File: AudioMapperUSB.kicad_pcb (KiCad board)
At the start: 2 copper layers, 100 x 100 mm, 155 parts, among them J1 USB_B, J10 Conn_01x01, J11 Conn_01x01, J12 Jack-DC, J16 Audio-Jack-2, J17 Audio-Jack-2, J18 Audio-Jack-2, J19 Audio-Jack-2, J2 Audio-Jack-2, J20 Audio-Jack-2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

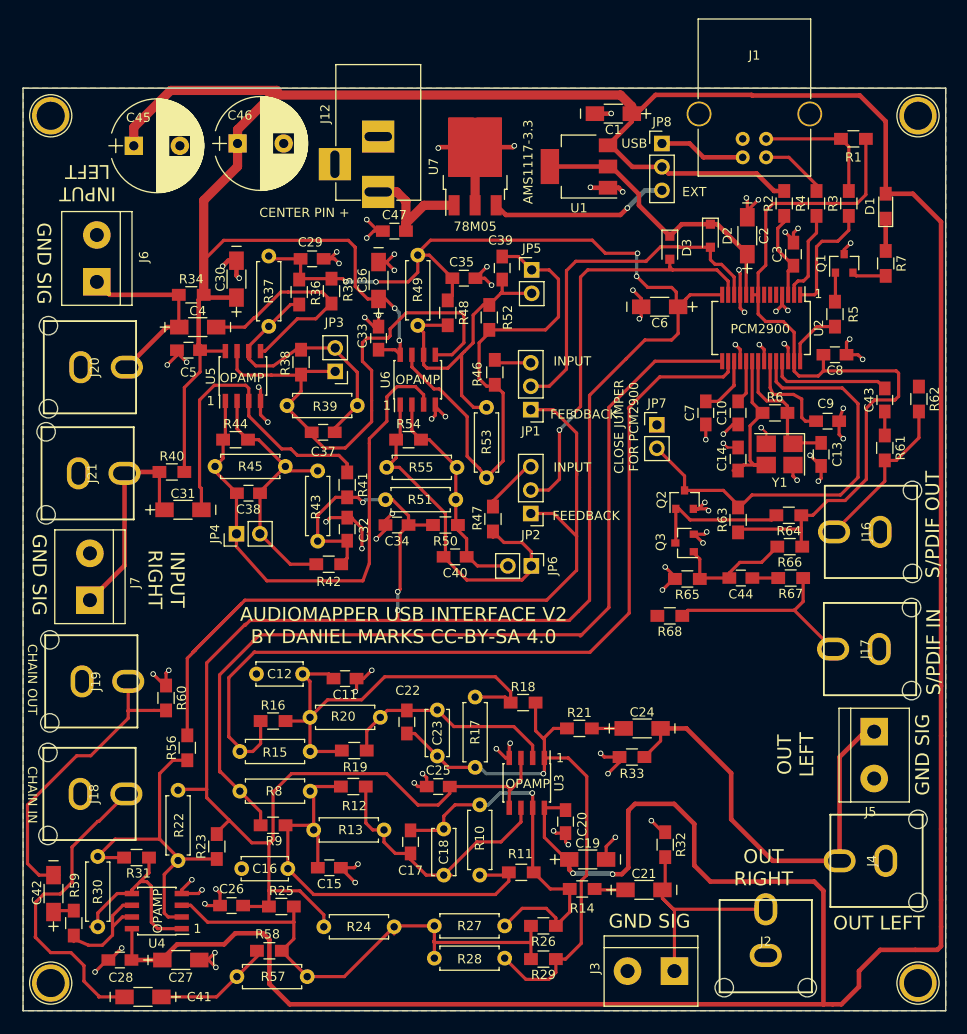
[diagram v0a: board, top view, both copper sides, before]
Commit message: Use inverter for SPDIF
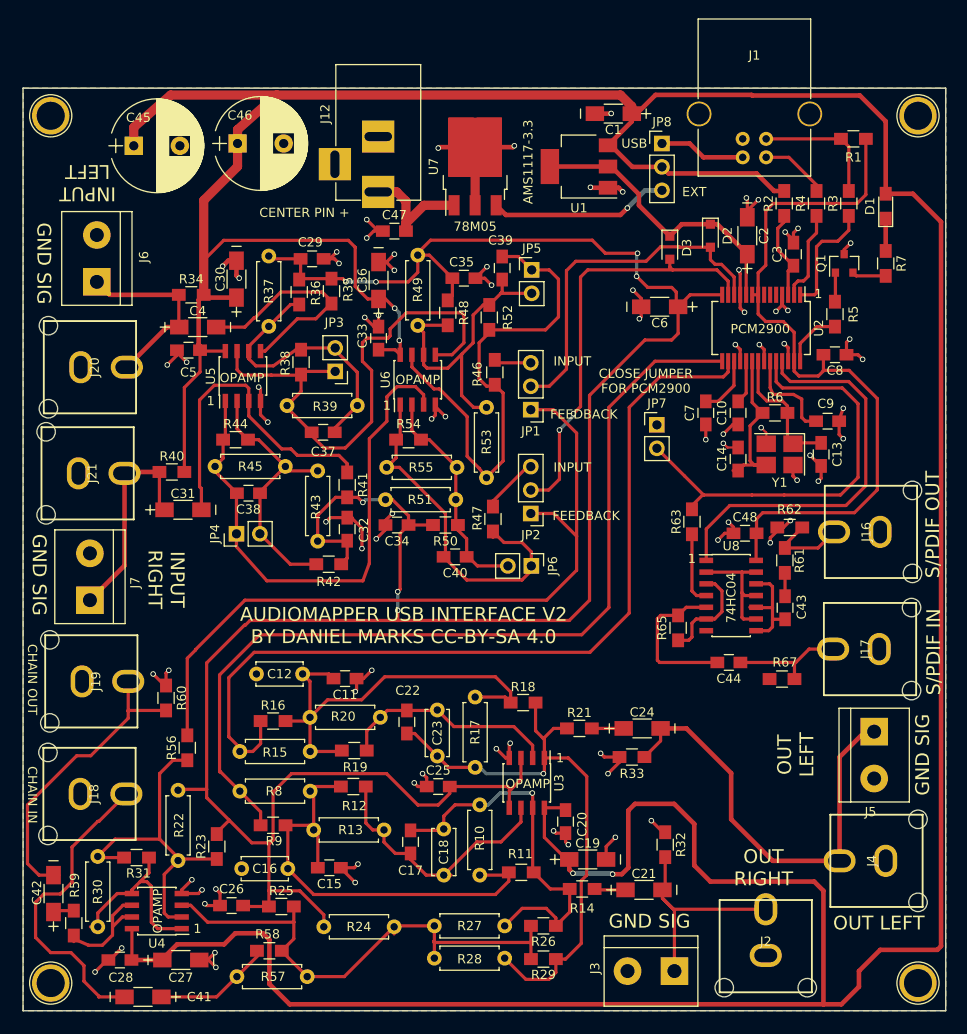
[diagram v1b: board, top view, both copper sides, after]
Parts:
- removed Q2, Q3: MMBT3904, TO_SOT_Packages_SMD:SOT-23
- removed R64: 1k, Resistors_SMD:R_0805_HandSoldering
- removed R66: 100k, Resistors_SMD:R_0805_HandSoldering
- removed R68: NC, Resistors_SMD:R_0805_HandSoldering
- added C48: 1 uF, Capacitors_SMD:C_0805_HandSoldering, F.Cu at (108.2, 78.2)
- added U8: 74HC04, Housings_SOIC:SOIC-14_3.9x8.7mm_Pitch1.27mm, F.Cu at (106.8, 85.0)
- R52, R54: value 100k -> 22k
- R65: value 10k -> 100k
- moved C43 25.0 mm to (112.6, 86.3), turned to 270 degrees
- moved R62 19.7 mm to (113.1, 77.6), turned to 0 degrees
- moved R61 16.3 mm to (112.6, 81.2), turned to 90 degrees
- moved R67 11.0 mm to (112.3, 94.0)
- moved C44 9.24 mm to (106.5, 92.2)
- moved R65 5.39 mm to (101.0, 88.5), turned to 270 degrees
- moved R63 5.00 mm to (102.5, 77.0)
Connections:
- C8 pad 1: Net-(C8-Pad1) -> VDDI
- J17 pad 1: Net-(J17-Pad1) -> Net-(C44-Pad1)
- R1 pad 2: Net-(C8-Pad1) -> VDDI
- R63 pad 1: Net-(C8-Pad1) -> Net-(R63-Pad1)
- R65 pad 2: GND -> Net-(R65-Pad2)
- R67 pad 1: Net-(J17-Pad1) -> Net-(C44-Pad1)
- R67 pad 2: Net-(C44-Pad1) -> GND
- U2 pad 25: Net-(C43-Pad2) -> Net-(U2-Pad25)
- U2 pad 27: Net-(C8-Pad1) -> VDDI
- U2 pad 8: Net-(C8-Pad1) -> VDDI
- U2 pad 9: Net-(C8-Pad1) -> VDDI
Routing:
- net Net-(C8-Pad1): track 86.2 -> 0.00 mm
- net VDDI: track 0.00 -> 80.8 mm
- net Net-(U2-Pad25): track 0.00 -> 43.6 mm
- net Net-(J17-Pad1): track 22.2 -> 0.00 mm
- net Net-(Q2-Pad1): track 15.3 -> 0.00 mm
- net Net-(U8-Pad11): track 0.00 -> 13.7 mm
- net Net-(R65-Pad2): track 0.00 -> 11.2 mm
- net Net-(C44-Pad1): track 2.80 -> 12.5 mm
- net Net-(J16-Pad1): track 17.6 -> 9.30 mm
- net Net-(JP1-Pad1): track 89.5 -> 81.4 mm
- net Net-(R63-Pad1): track 0.00 -> 7.91 mm
- net GND: track 174.8 -> 171.2 mm, vias 82 -> 80
- net Net-(C44-Pad2): track 13.4 -> 16.9 mm
- net Net-(C1-Pad1): track 466.7 -> 464.8 mm
- net Net-(C43-Pad2): track 13.3 -> 12.1 mm
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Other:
- board text added: "74HC04"

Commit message: Fixed problem with VCOM leaking into input audio
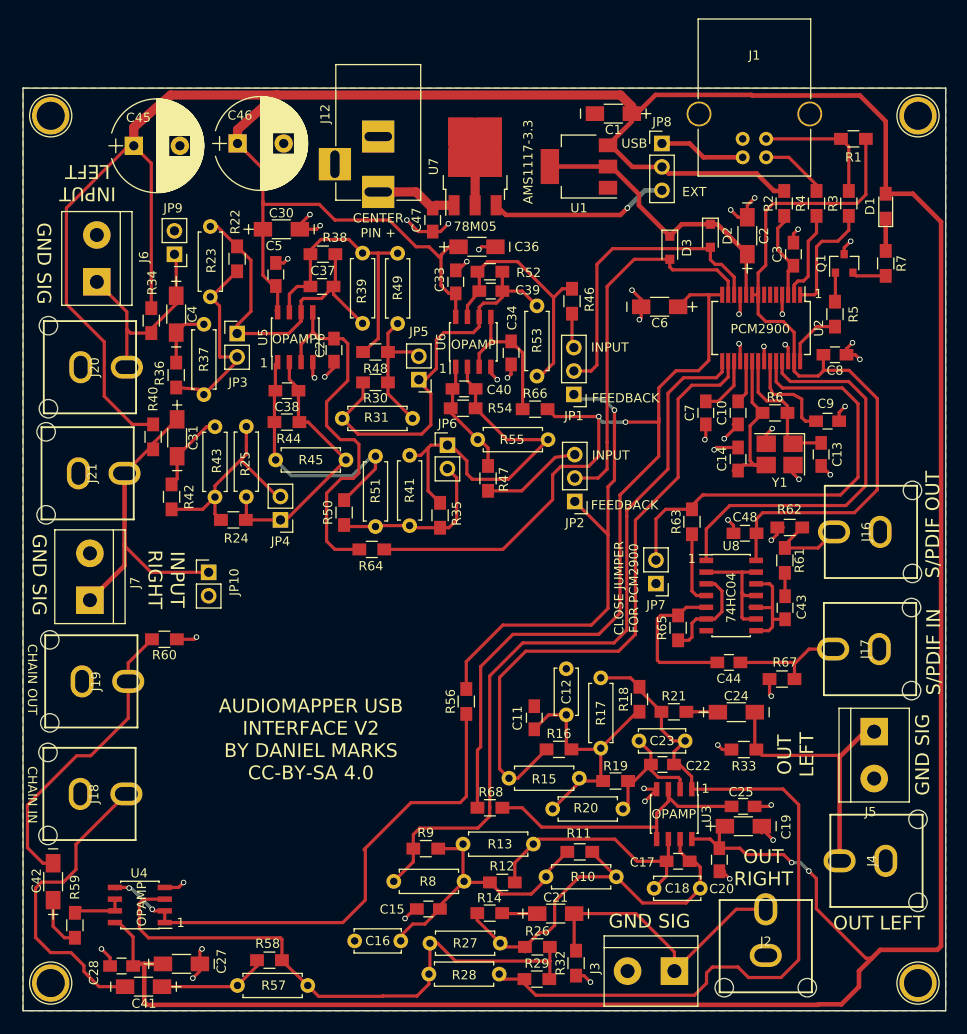
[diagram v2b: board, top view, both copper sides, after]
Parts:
- removed C29, C32, C35: 1 uF, Capacitors_SMD:C_0805_HandSoldering
- added JP10: Jumper_NO_Small, Pin_Headers:Pin_Header_Straight_1x02_Pitch2.54mm, F.Cu at (50.1, 82.5)
- added JP9: Jumper_NO_Small, Pin_Headers:Pin_Header_Straight_1x02_Pitch2.54mm, F.Cu at (46.4, 48.0)
- added R64: 100k, Resistors_SMD:R_0805_HandSoldering, F.Cu at (67.8, 80.0)
- added R66: 100k, Resistors_SMD:R_0805_HandSoldering, F.Cu at (85.5, 64.8)
- added R68: 100k, Resistors_SMD:R_0805_HandSoldering, F.Cu at (80.6, 108.0)
- C39, C40: value 22 pF -> 100 pF
- JP3, JP4, JP5, JP6: value Jumper_NO_Small -> Jumper_NC_Small
- R22, R24: value NO -> 100k; footprint Resistors_THT:R_Axial_DIN0207_L6.3mm_D2.5mm_P7.62mm_Horizontal -> Resistors_SMD:R_0805_HandSoldering
- R23, R25: value 10k -> NO; footprint Resistors_SMD:R_0805_HandSoldering -> Resistors_THT:R_Axial_DIN0207_L6.3mm_D2.5mm_P7.62mm_Horizontal
- R30: value NO -> 18k; footprint Resistors_THT:R_Axial_DIN0207_L6.3mm_D2.5mm_P7.62mm_Horizontal -> Resistors_SMD:R_0805_HandSoldering
- R31: value 0R -> NO; footprint Resistors_SMD:R_0805_HandSoldering -> Resistors_THT:R_Axial_DIN0207_L6.3mm_D2.5mm_P7.62mm_Horizontal
- R35: value 100k -> 18k
- R41: value 100k -> NO; footprint Resistors_SMD:R_0805_HandSoldering -> Resistors_THT:R_Axial_DIN0207_L6.3mm_D2.5mm_P7.62mm_Horizontal
- R65: value 100k -> 10k
- moved R23 67.2 mm to (50.3, 45.0), turned to 270 degrees
- moved R30 66.2 mm to (68.2, 61.9), turned to 180 degrees
- moved C26 61.2 mm to (63.7, 58.4), turned to 270 degrees
- moved R22 58.0 mm to (53.2, 48.5), turned to 90 degrees
- moved R31 52.6 mm to (64.6, 65.8)
- moved R24 45.2 mm to (52.8, 76.8)
- moved R25 44.6 mm to (54.2, 74.3), turned to 90 degrees
- moved C12 33.6 mm to (88.9, 92.9), turned to 270 degrees
- moved C25 33.1 mm to (108.0, 107.8), turned to 180 degrees
- moved R16 31.1 mm to (88.1, 101.7)
- moved R56 30.7 mm to (78.0, 96.5)
- moved R15 29.3 mm to (82.7, 104.8)
- moved C17 29.1 mm to (101.0, 113.8), turned to 0 degrees
- moved R19 28.5 mm to (94.2, 105.1)
- moved R20 28.1 mm to (87.4, 108.1)
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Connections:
- C25 pad 2: VCOM -> Net-(C25-Pad2)
- C26 pad 1: GND -> Net-(C26-Pad1)
- C26 pad 2: VCOM -> GND
- C34 pad 1: GND -> Net-(C34-Pad1)
- C34 pad 2: VCOM -> GND
- JP3 pad 1: Net-(C37-Pad2) -> Net-(C37-Pad1)
- JP3 pad 2: Net-(C37-Pad1) -> Net-(JP3-Pad2)
- JP4 pad 1: Net-(C38-Pad2) -> Net-(C38-Pad1)
- JP4 pad 2: Net-(C38-Pad1) -> Net-(JP4-Pad2)
- JP5 pad 1: Net-(C39-Pad2) -> Net-(C39-Pad1)
- JP5 pad 2: Net-(C39-Pad1) -> Net-(JP5-Pad2)
- JP6 pad 1: Net-(C40-Pad2) -> Net-(C40-Pad1)
- JP6 pad 2: Net-(C40-Pad1) -> Net-(JP6-Pad2)
- R22 pad 1: VCOM -> Net-(JP3-Pad2)
- R22 pad 2: Net-(R22-Pad2) -> Net-(C37-Pad1)
- R23 pad 1: Net-(R22-Pad2) -> Net-(C37-Pad1)
- R23 pad 2: VCOM -> Net-(JP3-Pad2)
- R24 pad 1: VCOM -> Net-(JP4-Pad2)
- R24 pad 2: Net-(R24-Pad2) -> Net-(C38-Pad1)
- R25 pad 1: Net-(R24-Pad2) -> Net-(C38-Pad1)
- R25 pad 2: VCOM -> Net-(JP4-Pad2)
- R26 pad 2: Net-(R24-Pad2) -> Net-(R26-Pad2)
- R27 pad 2: Net-(R24-Pad2) -> Net-(R26-Pad2)
- R28 pad 2: Net-(R24-Pad2) -> Net-(R26-Pad2)
- R29 pad 2: Net-(R24-Pad2) -> Net-(R26-Pad2)
- R30 pad 1: Net-(R30-Pad1) -> Net-(JP5-Pad2)
- R30 pad 2: Net-(R22-Pad2) -> Net-(C39-Pad1)
- R31 pad 1: Net-(R22-Pad2) -> Net-(C39-Pad1)
- R31 pad 2: Net-(R30-Pad1) -> Net-(JP5-Pad2)
- R35 pad 1: Net-(C4-Pad2) -> Net-(JP6-Pad2)
- R35 pad 2: VCOM -> Net-(C40-Pad1)
- R36 pad 1: Net-(C37-Pad1) -> Net-(JP3-Pad2)
- R36 pad 2: VCOM -> Net-(C4-Pad2)
- R37 pad 1: VCOM -> Net-(C4-Pad2)
- R37 pad 2: Net-(C37-Pad1) -> Net-(JP3-Pad2)
- R41 pad 1: Net-(C31-Pad2) -> Net-(C40-Pad1)
- R41 pad 2: VCOM -> Net-(JP6-Pad2)
- R42 pad 1: Net-(C38-Pad1) -> Net-(JP4-Pad2)
- R42 pad 2: VCOM -> Net-(C31-Pad2)
- R43 pad 1: VCOM -> Net-(C31-Pad2)
- R43 pad 2: Net-(C38-Pad1) -> Net-(JP4-Pad2)
- R48 pad 1: Net-(C39-Pad1) -> Net-(JP5-Pad2)
- R48 pad 2: VCOM -> Net-(C37-Pad2)
- R49 pad 1: VCOM -> Net-(C37-Pad2)
- R49 pad 2: Net-(C39-Pad1) -> Net-(JP5-Pad2)
- R50 pad 1: Net-(C40-Pad1) -> Net-(JP6-Pad2)
- R50 pad 2: VCOM -> Net-(C38-Pad2)
- R51 pad 1: VCOM -> Net-(C38-Pad2)
- R51 pad 2: Net-(C40-Pad1) -> Net-(JP6-Pad2)
- R56 pad 1: Net-(R22-Pad2) -> Net-(R56-Pad1)
- R57 pad 1: Net-(R24-Pad2) -> Net-(R26-Pad2)
- R58 pad 1: Net-(R24-Pad2) -> Net-(R26-Pad2)
- U3 pad 3: VCOM -> Net-(C25-Pad2)
- U3 pad 5: VCOM -> Net-(C25-Pad2)
- U4 pad 1: Net-(R30-Pad1) -> Net-(R56-Pad1)
- U4 pad 2: Net-(R22-Pad2) -> Net-(R56-Pad1)
- U4 pad 3: Net-(R24-Pad2) -> Net-(R26-Pad2)
- U4 pad 5: Net-(R30-Pad1) -> Net-(R56-Pad1)
- U5 pad 3: Net-(C31-Pad2) -> Net-(C26-Pad1)
- U5 pad 5: Net-(C4-Pad2) -> Net-(C26-Pad1)
- U6 pad 3: Net-(C38-Pad2) -> Net-(C34-Pad1)
- U6 pad 5: Net-(C37-Pad2) -> Net-(C34-Pad1)
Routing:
- net VCOM: track 275.5 -> 125.1 mm, vias 7 -> 2
- net GND: track 171.2 -> 104.2 mm, vias 80 -> 47
- net Net-(R26-Pad2): track 0.00 -> 65.5 mm
- net Net-(R56-Pad1): track 0.00 -> 59.8 mm, vias 0 -> 2
- net Net-(R24-Pad2): track 58.2 -> 0.00 mm
- net Net-(C26-Pad1): track 0.00 -> 41.1 mm
- net Net-(R22-Pad2): track 37.4 -> 0.00 mm
- net Net-(C25-Pad2): track 0.00 -> 32.1 mm
- net Net-(C38-Pad2): track 59.7 -> 29.3 mm
- net Net-(JP1-Pad1): track 81.4 -> 52.7 mm, vias 0 -> 1
- net Net-(C37-Pad2): track 58.6 -> 30.6 mm
- net Net-(C40-Pad2): track 40.1 -> 12.8 mm
- net Net-(C39-Pad2): track 55.4 -> 28.4 mm
- net Net-(C31-Pad2): track 35.6 -> 8.72 mm
- net VOUTL: track 95.6 -> 68.9 mm
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
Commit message: Added isolation between phantom power in mic channels
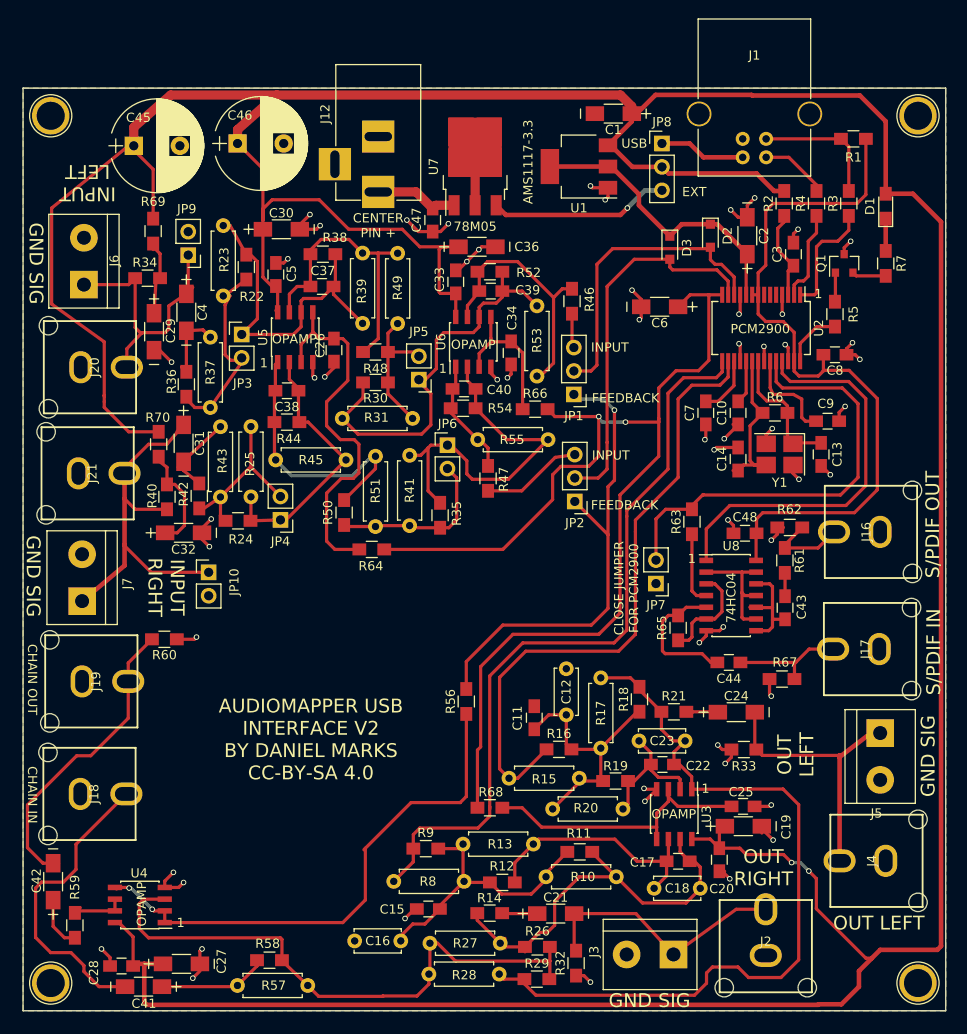
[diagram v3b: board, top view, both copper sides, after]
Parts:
- added C29: 10 uF, AudioMapperUSB:CP_1206_HandSoldering, F.Cu at (44.2, 56.4)
- added C32: 10 uF, AudioMapperUSB:CP_1206_HandSoldering, F.Cu at (47.4, 78.2)
- added R69: 1k, Resistors_SMD:R_0805_HandSoldering, F.Cu at (44.1, 45.5)
- added R70: 1k, Resistors_SMD:R_0805_HandSoldering, F.Cu at (44.7, 68.6)
- R34, R40: value 10k -> 4k7
- moved R40 6.67 mm to (45.6, 74.3)
- moved R34 4.62 mm to (43.5, 50.6), turned to 0 degrees
- moved R42 3.00 mm to (49.1, 74.2)
- moved J3 1.80 mm to (100.5, 123.9)
- moved R37 1.57 mm to (50.3, 57.0)
- moved JP9 1.49 mm to (47.9, 48.1)
- moved R36 1.49 mm to (47.7, 62.1)
- moved J6 1.43 mm to (36.6, 51.3)
- moved R23 1.40 mm to (51.7, 44.9)
- moved R22 1.35 mm to (54.2, 49.4)
- moved C4 1.12 mm to (47.7, 54.3)
- moved C31 0.92 mm to (47.4, 68.5)
- moved J7 0.86 mm to (36.4, 85.6)
- moved J5 0.67 mm to (122.9, 99.9)
- moved R43 0.60 mm to (51.4, 66.7)
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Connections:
- R34 pad 2: Net-(C1-Pad1) -> Net-(C29-Pad1)
- R40 pad 2: Net-(C1-Pad1) -> Net-(C32-Pad1)
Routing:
- net GND: track 104.2 -> 123.8 mm, vias 47 -> 56
- net Net-(C32-Pad1): track 0.00 -> 12.1 mm
- net Net-(C4-Pad1): track 23.1 -> 32.8 mm
- net Net-(C31-Pad1): track 34.6 -> 44.1 mm
- net Net-(C29-Pad1): track 0.00 -> 8.70 mm
- net Net-(JP4-Pad2): track 23.0 -> 19.5 mm
- net Net-(C21-Pad2): track 31.4 -> 28.7 mm
- net Net-(C4-Pad2): track 6.62 -> 9.22 mm
- net Net-(C44-Pad2): track 16.9 -> 15.1 mm
- net Net-(C31-Pad2): track 8.72 -> 10.3 mm
- net Net-(C1-Pad1): track 458.7 -> 457.4 mm

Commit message: JLCPCB order 2021-01-31
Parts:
- added J13: Conn_01x02, Connectors_Terminal_Blocks:TerminalBlock_bornier-2_P5.08mm, F.Cu at (58.8, 123.2)
- added J14: Conn_01x02, Connectors_Terminal_Blocks:TerminalBlock_bornier-2_P5.08mm, F.Cu at (37.4, 114.4)
- moved R56 23.7 mm to (55.9, 105.0), turned to 0 degrees
- moved C41 21.0 mm to (61.7, 117.7)
- moved C28 18.7 mm to (56.1, 114.6), turned to 180 degrees
- moved R59 18.2 mm to (50.2, 109.8)
- moved J18 17.8 mm to (44.2, 122.9), turned to 180 degrees
- moved U4 15.8 mm to (56.0, 110.1)
- moved R58 15.2 mm to (62.5, 110.5), turned to 270 degrees
- moved C42 15.0 mm to (46.5, 108.9)
- moved R60 12.4 mm to (46.5, 102.1), turned to 270 degrees
- moved C27 10.5 mm to (48.8, 114.5), turned to 180 degrees
- moved R57 10.1 mm to (70.9, 126.0)
- moved J19 5.12 mm to (37.9, 99.4)
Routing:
- net Net-(R56-Pad1): track 59.8 -> 11.4 mm, vias 2 -> 0
- net Net-(JP1-Pad1): track 52.7 -> 82.0 mm
- net GND: track 123.8 -> 144.6 mm, vias 56 -> 66
- net Net-(C41-Pad2): track 33.3 -> 20.6 mm
- net Net-(R26-Pad2): track 65.5 -> 54.1 mm
- net Net-(C42-Pad2): track 34.0 -> 23.0 mm
- net Net-(C1-Pad1): track 457.4 -> 452.9 mm
- net Net-(R59-Pad1): track 8.59 -> 4.79 mm
- net Net-(C42-Pad1): track 6.75 -> 3.80 mm
- net Net-(C41-Pad1): track 12.5 -> 15.3 mm
